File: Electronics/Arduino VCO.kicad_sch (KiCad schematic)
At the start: 45 parts, among them U1 TL072

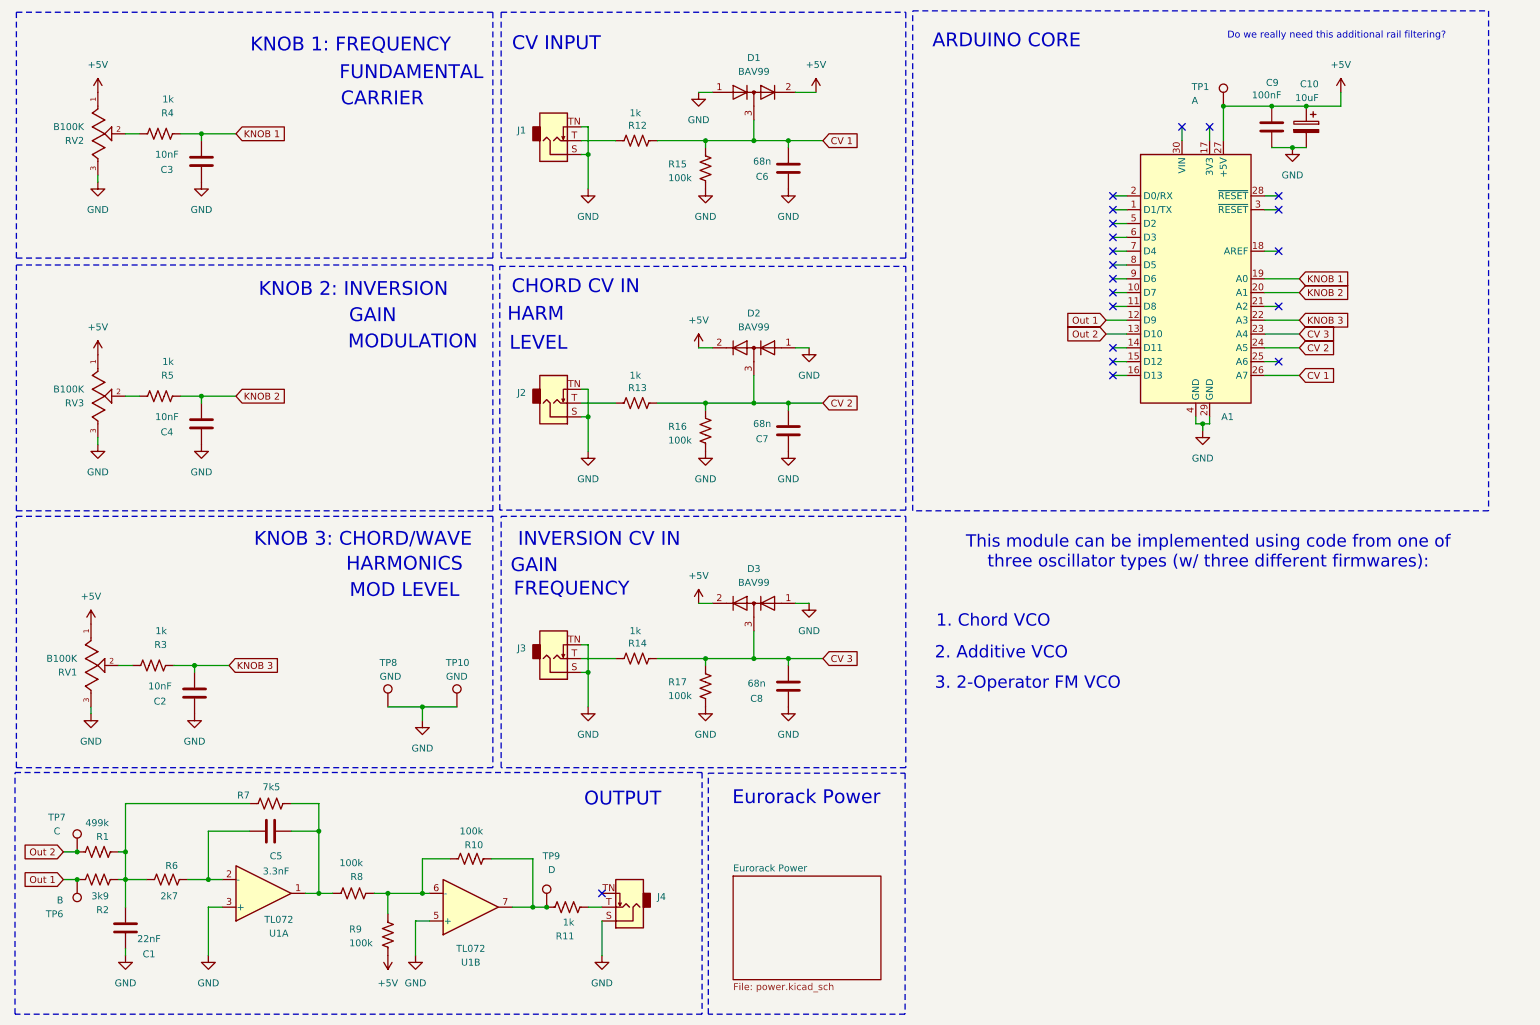
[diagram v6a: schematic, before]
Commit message: creating a 6HP PCB panel
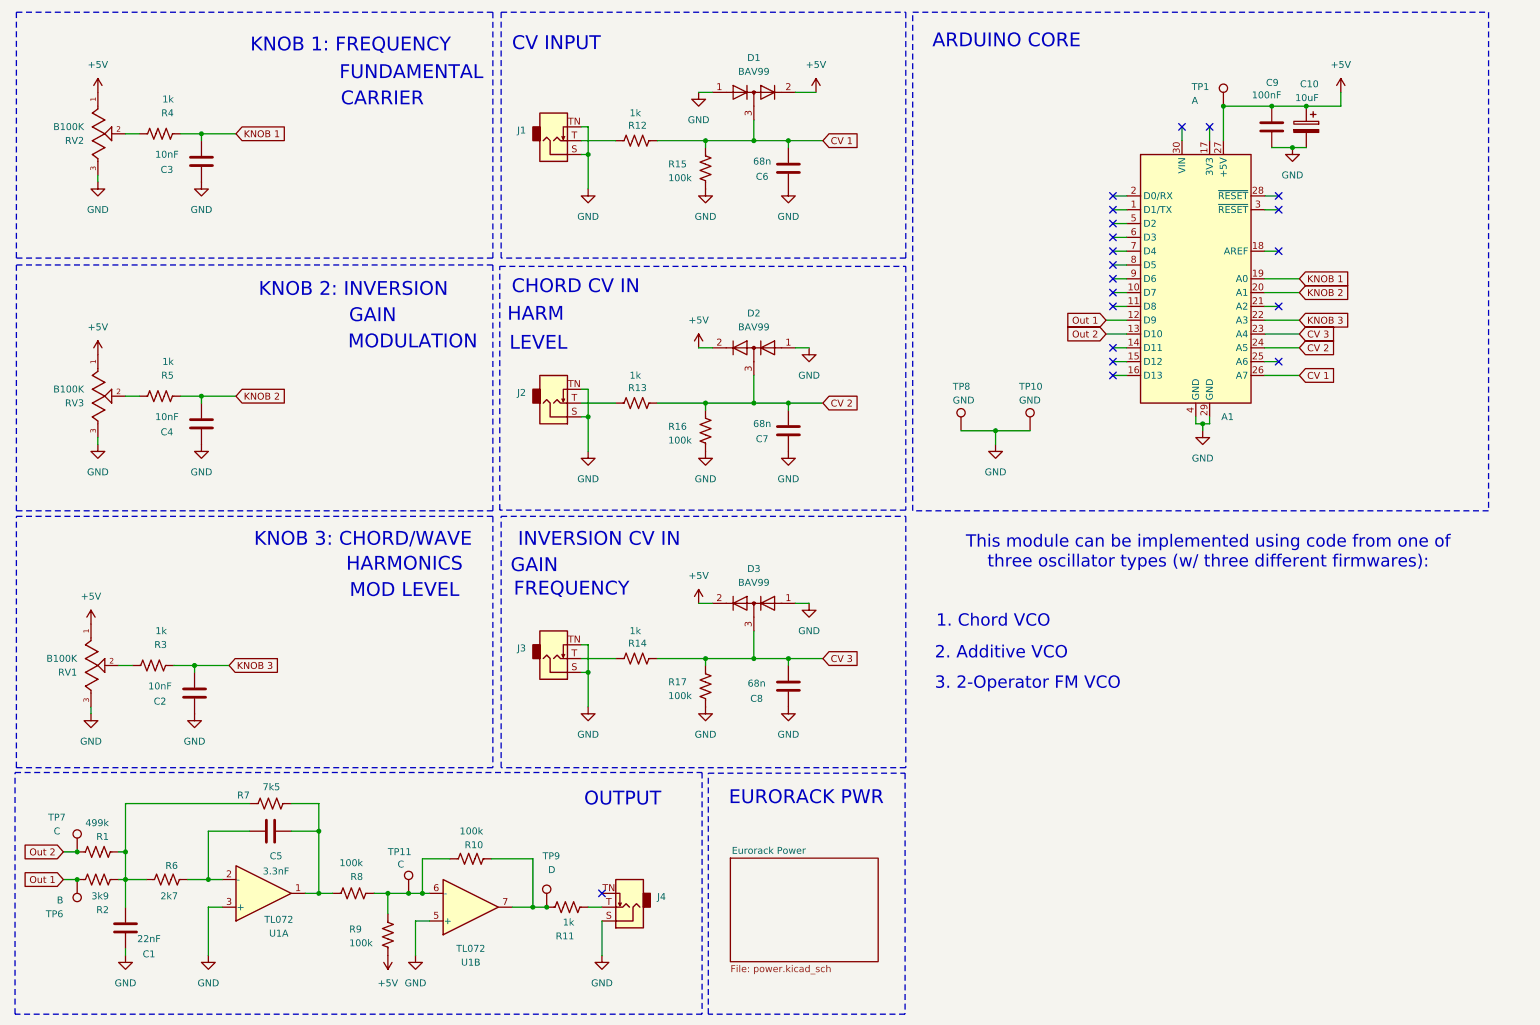
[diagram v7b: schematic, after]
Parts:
- added TP11: C, TestPoint:TestPoint_Pad_D1.5mm, symbol Connector:TestPoint
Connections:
- net at R10.1, R8.2, R9.2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: now also TP11.1
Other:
- note added: "EURORACK PWR"
- note removed: "Do we really need this additional rail filtering?"
- note removed: "Eurorack Power"
- moved on the sheet: TP10, TP8
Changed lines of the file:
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@@
 	(title_block
 		(title "CY3-FOLD VCO")
-		(date "2026-04-17")
+		(date "2026-05-18")
 		(rev "v1.0")
 		(company "©Dirty Dream - Nathanael Noir")
@@
 	)
 	(rectangle
-		(start 177.8 12.954)
+		(start 177.8 13.208)
 		(end 283.718 104.902)
 		(stroke
@@
 		)
 	)
-	(text "Eurorack Power\n"
+	(text "EURORACK PWR\n"
 		(exclude_from_sim no)
 		(at 158.242 157.734 0)
@@
 		)
 	)
-	(text "Do we really need this additional rail filtering?"
-		(exclude_from_sim no)
-		(at 255.778 17.526 0)
-		(effects
-			(font
-				(size 1.27 1.27)
-				(color 255 0 0 1)
-			)
-		)
-	)
 	(text "MODULATION\n"
 		(exclude_from_sim no)
@@
 	)
 	(junction
-		(at 87.63 140.97)
+		(at 193.04 90.17)
 		(diameter 0)
 		(color 0 0 0 0)
@@
 	)
 	(junction
+		(at 85.09 175.26)
+		(diameter 0)
+		(color 0 0 0 0)
+	)
+	(junction
 		(at 46.99 35.56)
 		(diameter 0)
@@
 	(wire
 		(pts
+			(xy 85.09 175.26) (xy 87.63 175.26)
+		)
+		(stroke
+			(width 0)
+			(type default)
+		)
+	)
+	(wire
+		(pts
 			(xy 247.65 38.1) (xy 250.19 38.1)
 		)
@@
 	(wire
 		(pts
-			(xy 87.63 140.97) (xy 93.98 140.97)
+			(xy 193.04 90.17) (xy 199.39 90.17)
 		)
 		(stroke
@@
 	(wire
 		(pts
-			(xy 87.63 143.51) (xy 87.63 140.97)
+			(xy 193.04 92.71) (xy 193.04 90.17)
 		)
 		(stroke
@@
 	(wire
 		(pts
-			(xy 81.28 140.97) (xy 87.63 140.97)
+			(xy 186.69 90.17) (xy 193.04 90.17)
 		)
 		(stroke
@@
 	(wire
 		(pts
-			(xy 81.28 175.26) (xy 87.63 175.26)
+			(xy 81.28 175.26) (xy 85.09 175.26)
 		)
 		(stroke
@@
 	(symbol
 		(lib_id "Connector:TestPoint")
-		(at 93.98 140.97 0)
+		(at 199.39 90.17 0)
 		(unit 1)
 		(body_style 1)
@@
 		(dnp no)
 		(property "Reference" "TP10"
-			(at 91.948 132.842 0)
+			(at 197.358 82.042 0)
 			(show_name no)
 			(do_not_autoplace no)
@@
 		)
 		(property "Value" "GND"
-			(at 91.948 135.382 0)
+			(at 197.358 84.582 0)
 			(show_name no)
 			(do_not_autoplace no)
@@
 		)
 		(property "Footprint" "TestPoint:TestPoint_Pad_D1.5mm"
-			(at 99.06 140.97 0)
+			(at 204.47 90.17 0)
 			(hide yes)
 			(show_name no)
@@
 		)
 		(property "Datasheet" ""
-			(at 99.06 140.97 0)
+			(at 204.47 90.17 0)
 			(hide yes)
 			(show_name no)
@@
 		)
 		(property "Description" "test point"
-			(at 93.98 140.97 0)
+			(at 199.39 90.17 0)
 			(hide yes)
 			(show_name no)
@@
 	(symbol
 		(lib_id "power:GND")
-		(at 87.63 143.51 0)
+		(at 193.04 92.71 0)
 		(unit 1)
 		(body_style 1)
@@
 		(fields_autoplaced yes)
 		(property "Reference" "#PWR042"
-			(at 87.63 149.86 0)
+			(at 193.04 99.06 0)
 			(hide yes)
 			(show_name no)
@@
 		)
 		(property "Value" "GND"
-			(at 87.63 148.59 0)
+			(at 193.04 97.79 0)
 			(show_name no)
 			(do_not_autoplace no)
@@
 		)
 		(property "Footprint" ""
-			(at 87.63 143.51 0)
+			(at 193.04 92.71 0)
 			(hide yes)
 			(show_name no)
@@
 		)
 		(property "Datasheet" ""
-			(at 87.63 143.51 0)
+			(at 193.04 92.71 0)
 			(hide yes)
 			(show_name no)
@@
 		)
 		(property "Description" "Power symbol creates a global label with name \"GND\" , ground"
-			(at 87.63 143.51 0)
+			(at 193.04 92.71 0)
 			(hide yes)
 			(show_name no)
@@
 	(symbol
 		(lib_id "Connector:TestPoint")
-		(at 81.28 140.97 0)
+		(at 186.69 90.17 0)
 		(unit 1)
 		(body_style 1)
@@
 		(dnp no)
 		(property "Reference" "TP8"
-			(at 79.756 132.842 0)
+			(at 185.166 82.042 0)
 			(show_name no)
 			(do_not_autoplace no)
@@
 		)
 		(property "Value" "GND"
-			(at 79.756 135.382 0)
+			(at 185.166 84.582 0)
 			(show_name no)
 			(do_not_autoplace no)
@@
 		)
 		(property "Footprint" "TestPoint:TestPoint_Pad_D1.5mm"
-			(at 86.36 140.97 0)
+			(at 191.77 90.17 0)
 			(hide yes)
 			(show_name no)
@@
 		)
 		(property "Datasheet" ""
-			(at 86.36 140.97 0)
+			(at 191.77 90.17 0)
 			(hide yes)
 			(show_name no)
@@
 		)
 		(property "Description" "test point"
-			(at 81.28 140.97 0)
+			(at 186.69 90.17 0)
 			(hide yes)
 			(show_name no)
@@
 		)
 	)
+	(symbol
+		(lib_id "Connector:TestPoint")
+		(at 85.09 175.26 0)
+		(unit 1)
+		(body_style 1)
+		(exclude_from_sim no)
+		(in_bom yes)
+		(on_board yes)
+		(in_pos_files yes)
+		(dnp no)
+		(property "Reference" "TP11"
+			(at 81.28 167.64 0)
+			(show_name no)
+			(do_not_autoplace no)
+			(effects
+				(font
+					(size 1.27 1.27)
+				)
+				(justify left)
+			)
+		)
+		(property "Value" "C"
+			(at 83.058 169.926 0)
+			(show_name no)
+			(do_not_autoplace no)
+			(effects
+				(font
+					(size 1.27 1.27)
+				)
+				(justify left)
+			)
+		)
+		(property "Footprint" "TestPoint:TestPoint_Pad_D1.5mm"
+			(at 90.17 175.26 0)
+			(hide yes)
+			(show_name no)
+			(do_not_autoplace no)
+			(effects
+				(font
+					(size 1.27 1.27)
+				)
+			)
+		)
+		(property "Datasheet" ""
+			(at 90.17 175.26 0)
+			(hide yes)
+			(show_name no)
+			(do_not_autoplace no)
+			(effects
+				(font
+					(size 1.27 1.27)
+				)
+			)
+		)
+		(property "Description" "test point"
+			(at 85.09 175.26 0)
+			(hide yes)
+			(show_name no)
+			(do_not_autoplace no)
+			(effects
+				(font
+					(size 1.27 1.27)
+				)
+			)
+		)
+		(pin "1"
+		)
+		(instances
+			(project "Arduino VCO"
+				(path "/3a28b572-943c-402b-9245-b62f72b0a8e3"
+					(reference "TP11")
+					(unit 1)
+				)
+			)
+		)
+	)
 	(sheet
-		(at 144.78 172.085)
+		(at 144.272 168.783)
 		(size 27.178 19.05)
 		(exclude_from_sim no)
@@
 		(on_board yes)
 		(dnp no)
-		(fields_autoplaced yes)
 		(stroke
 			(width 0.1524)
@@
 		)
 		(property "Sheetname" "Eurorack Power"
-			(at 144.78 171.3734 0)
+			(at 144.526 168.148 0)
 			(show_name no)
 			(do_not_autoplace no)
@@
 		)
 		(property "Sheetfile" "power.kicad_sch"
-			(at 144.78 191.7196 0)
+			(at 144.272 188.4176 0)
 			(show_name no)
 			(do_not_autoplace no)
